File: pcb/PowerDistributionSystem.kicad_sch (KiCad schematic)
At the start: 11 parts, among them J2 PREC040DBAN-M71RC, U1 TPS22810DRV, U2 D24V7F5, U3 D24V7F3

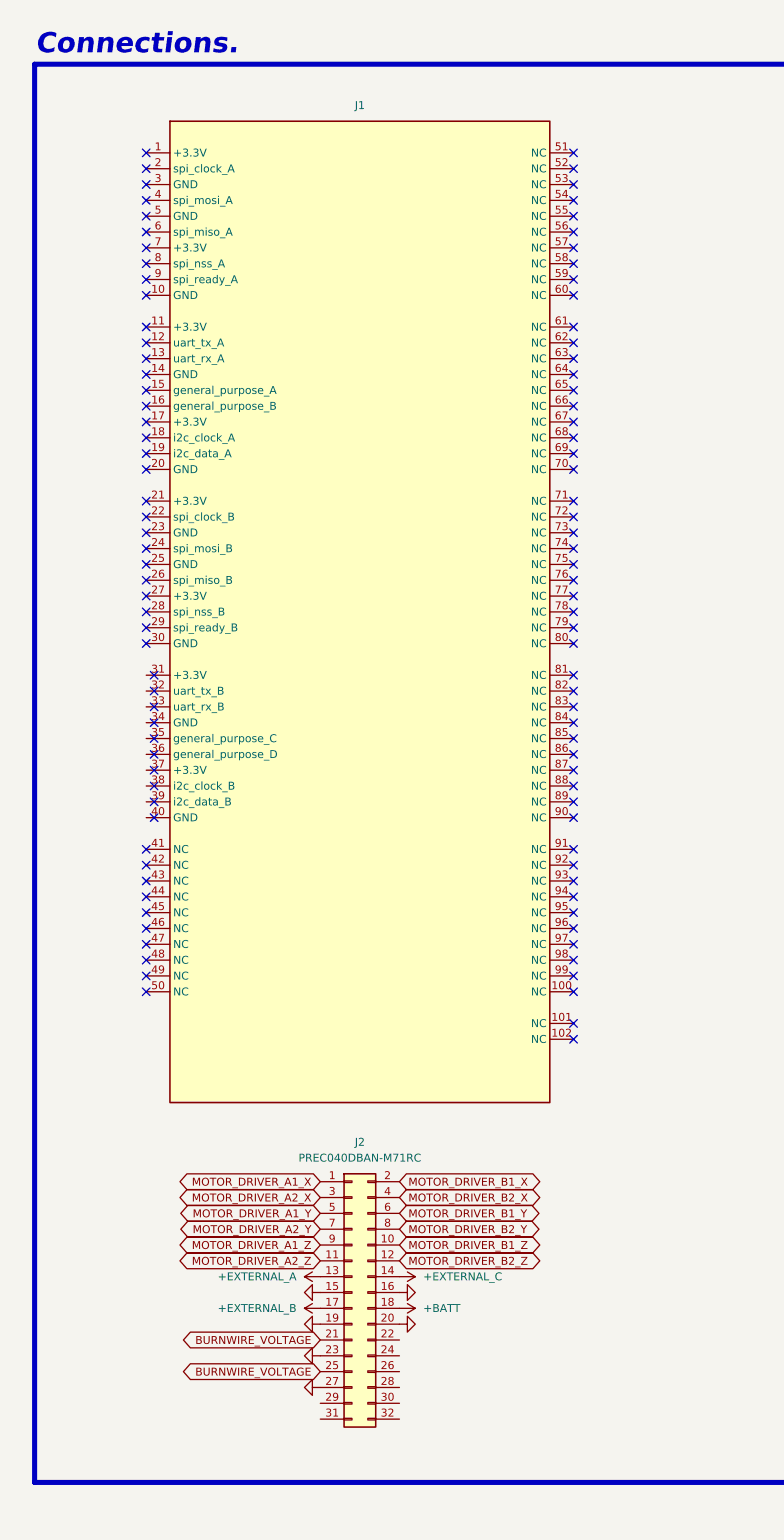
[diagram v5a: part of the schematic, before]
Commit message: Assigned some nets to the connectors.
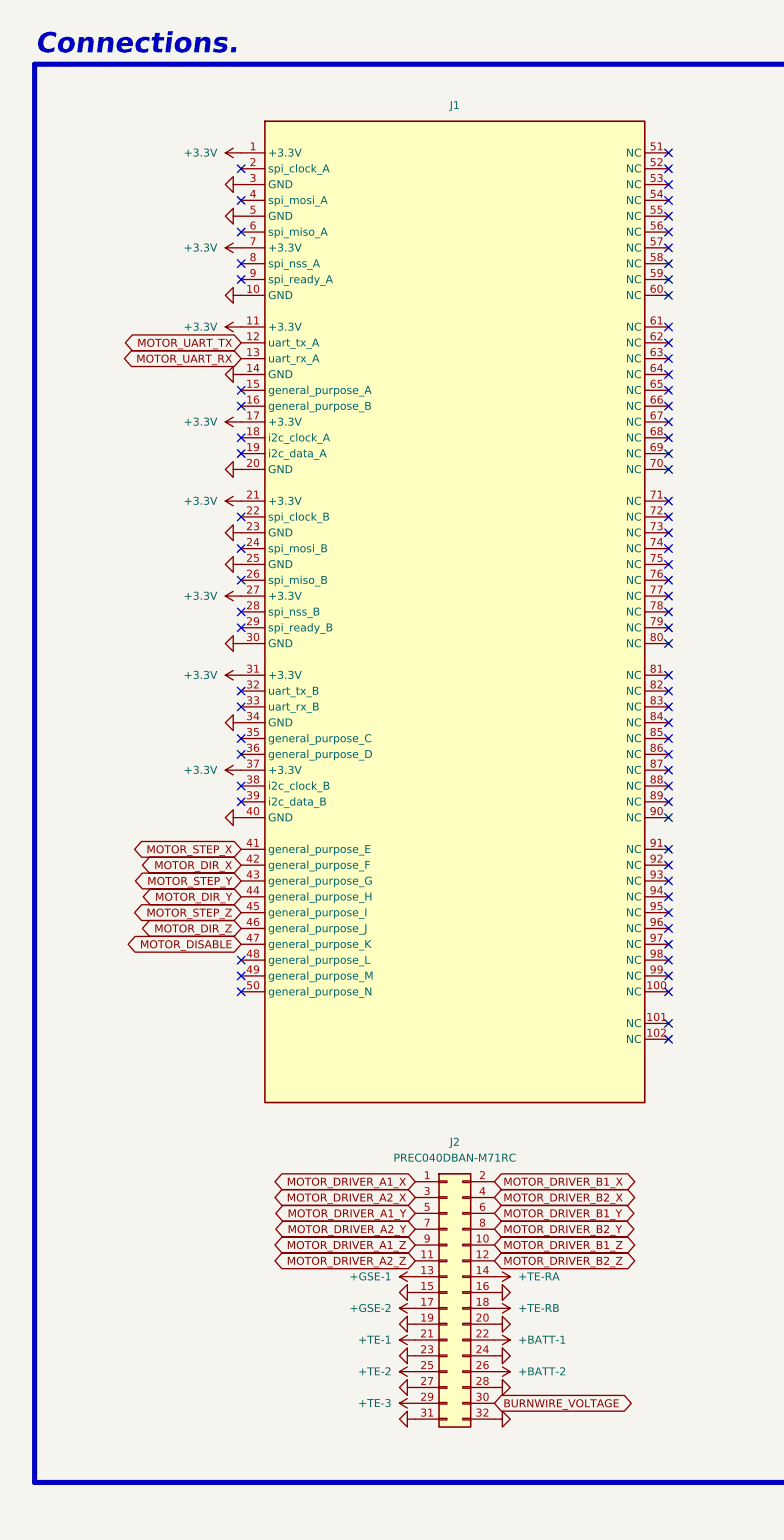
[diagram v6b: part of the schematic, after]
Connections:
- net +3.3V: now also J1.1 (+3.3V), J1.11 (+3.3V), J1.17 (+3.3V), J1.21 (+3.3V), J1.27 (+3.3V), J1.31 (+3.3V), J1.37 (+3.3V), J1.7 (+3.3V)
- net BURNWIRE_VOLTAGE: now also J2.30 (Pin_30); no longer J2.21 (Pin_21), J2.25 (Pin_25)
- net GND: now also J1.10 (GND), J1.14 (GND), J1.20 (GND), J1.23 (GND), J1.25 (GND), J1.3 (GND), J1.30 (GND), J1.34 (GND), J1.40 (GND), J1.5 (GND), J2.24 (Pin_24), J2.28 (Pin_28), J2.31 (Pin_31), J2.32 (Pin_32)
- net MOTOR_DIR_X: now also J1.42 (general_purpose_F)
- net MOTOR_DIR_Y: now also J1.44 (general_purpose_H)
- net MOTOR_DIR_Z: now also J1.46 (general_purpose_J)
- net MOTOR_DISABLE: now also J1.47 (general_purpose_K)
- net MOTOR_STEP_X: now also J1.41 (general_purpose_E)
- net MOTOR_STEP_Y: now also J1.43 (general_purpose_G)
- net MOTOR_STEP_Z: now also J1.45 (general_purpose_I)
- net MOTOR_UART_RX: now also J1.13 (uart_rx_A)
- net MOTOR_UART_TX: now also J1.12 (uart_tx_A)
- net +BATT-1: now reaches J2.22 (Pin_22)
- net +BATT-2: now reaches J2.26 (Pin_26)
- net +TE-3: now reaches J2.29 (Pin_29)
- net +BATT renamed +TE-RB
- net +EXTERNAL_A renamed +GSE-1
- net +EXTERNAL_B renamed +GSE-2
- net +EXTERNAL_C renamed +TE-RA
- new net +TE-1: J2.21 (Pin_21)
- new net +TE-2: J2.25 (Pin_25)
- no-connect marks 104 -> 77
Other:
- moved on the sheet: J1, J2

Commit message: Added regulators for burn-wire.
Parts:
- added R1: 1k, Resistor_SMD:R_1206_3216Metric_Pad1.30x1.75mm_HandSolder, symbol Device:R
- renumbered JP8 to JP1, JP1 to JP2, R1 to R2
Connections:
- net GND: now also R1.2
- new net BURNWIRE_ENABLE: R1.1
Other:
- added sheet Burnwire Regulator - 1 (PowerDistributionSystem_Burnwire_Regulator.kicad_sch)
- added sheet Burnwire Regulator - 2 (PowerDistributionSystem_Burnwire_Regulator.kicad_sch)
- added sheet Burnwire Regulator - 3 (PowerDistributionSystem_Burnwire_Regulator.kicad_sch)
- note added: "Active-low inhibit. @/pg 2/tbl 2/`L4978`."
- note added: "The L4978 can handle at least 2A (typically 3A). In case we need more power, having three L4978 in parallel will allow for at least 6A (although without current limit). We can look into a chip that can handle a higher current output later if need be."
- note added: "We can probably omit the decoupling capacitors for the input voltage."

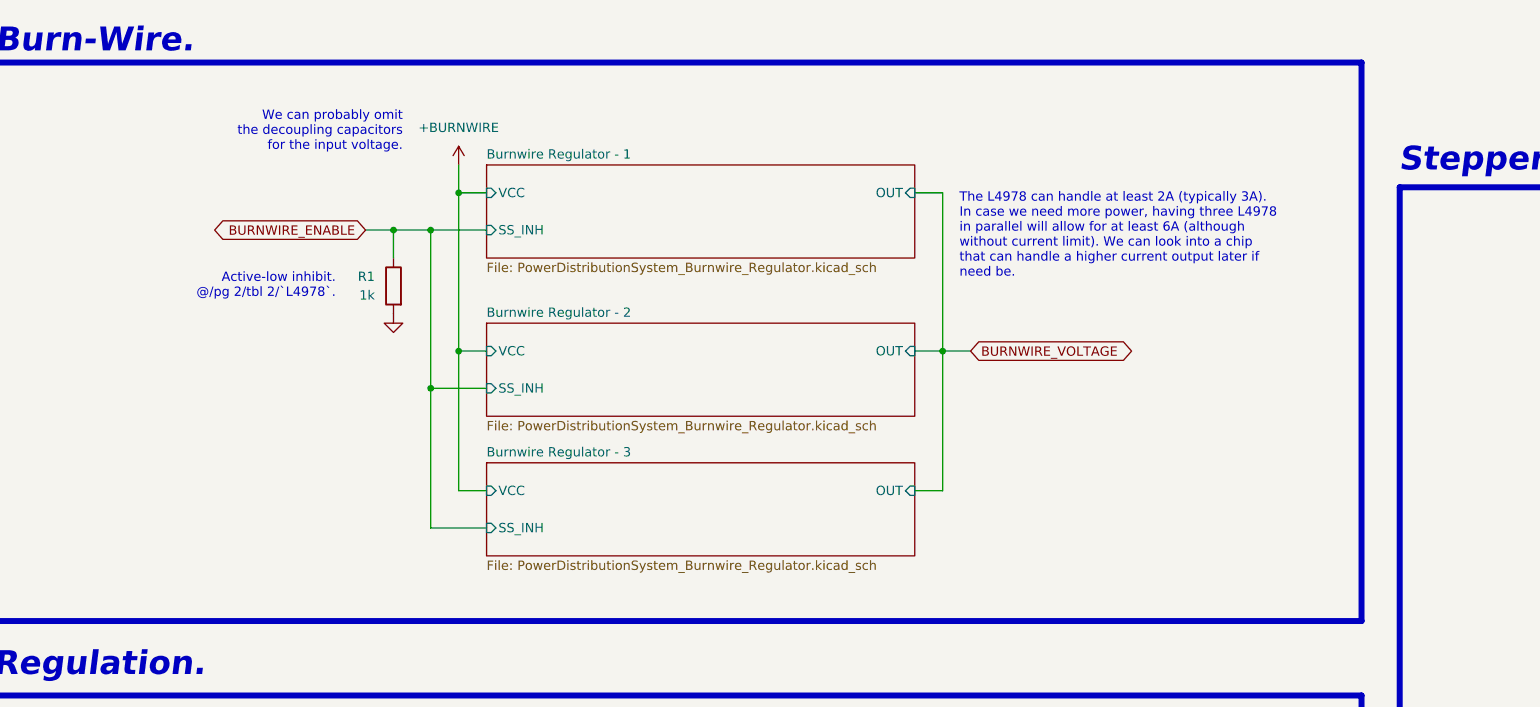
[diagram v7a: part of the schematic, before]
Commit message: Routed L4978 burn-wire regulators.
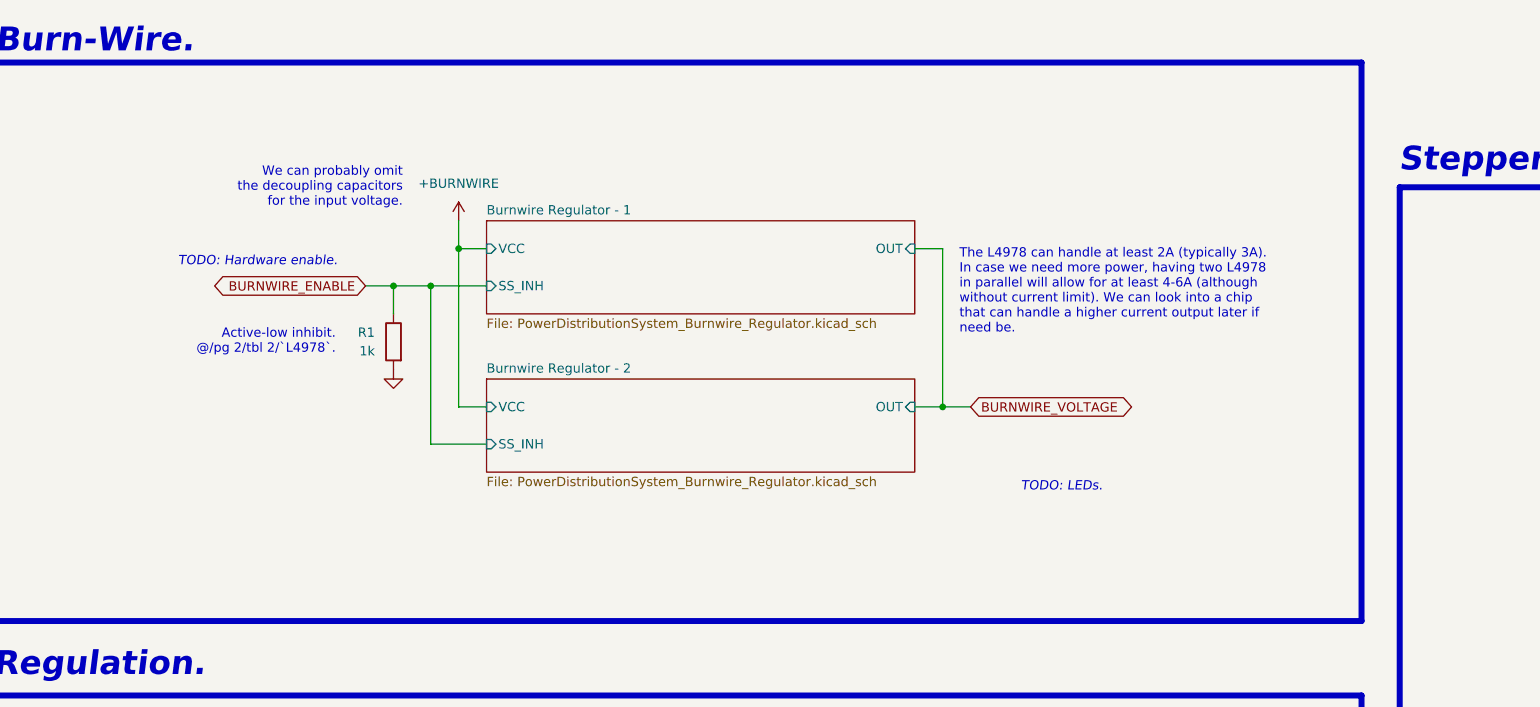
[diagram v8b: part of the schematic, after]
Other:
- removed sheet Burnwire Regulator - 3
- note added: "TODO: Hardware enable."
- note added: "TODO: LEDs."
- note added: "The L4978 can handle at least 2A (typically 3A). In case we need more power, having two L4978 in parallel will allow for at least 4-6A (although without current limit). We can look into a chip that can handle a higher current output later if need be."
- note removed: "The L4978 can handle at least 2A (typically 3A). In case we need more power, having three L4978 in parallel will allow for at least 6A (although without current limit). We can look into a chip that can handle a higher current output later if need be."
- moved on the sheet: R1
